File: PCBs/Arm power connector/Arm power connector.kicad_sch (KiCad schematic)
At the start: 11 parts, among them J1 Conn_01x08, J2 Conn_01x02

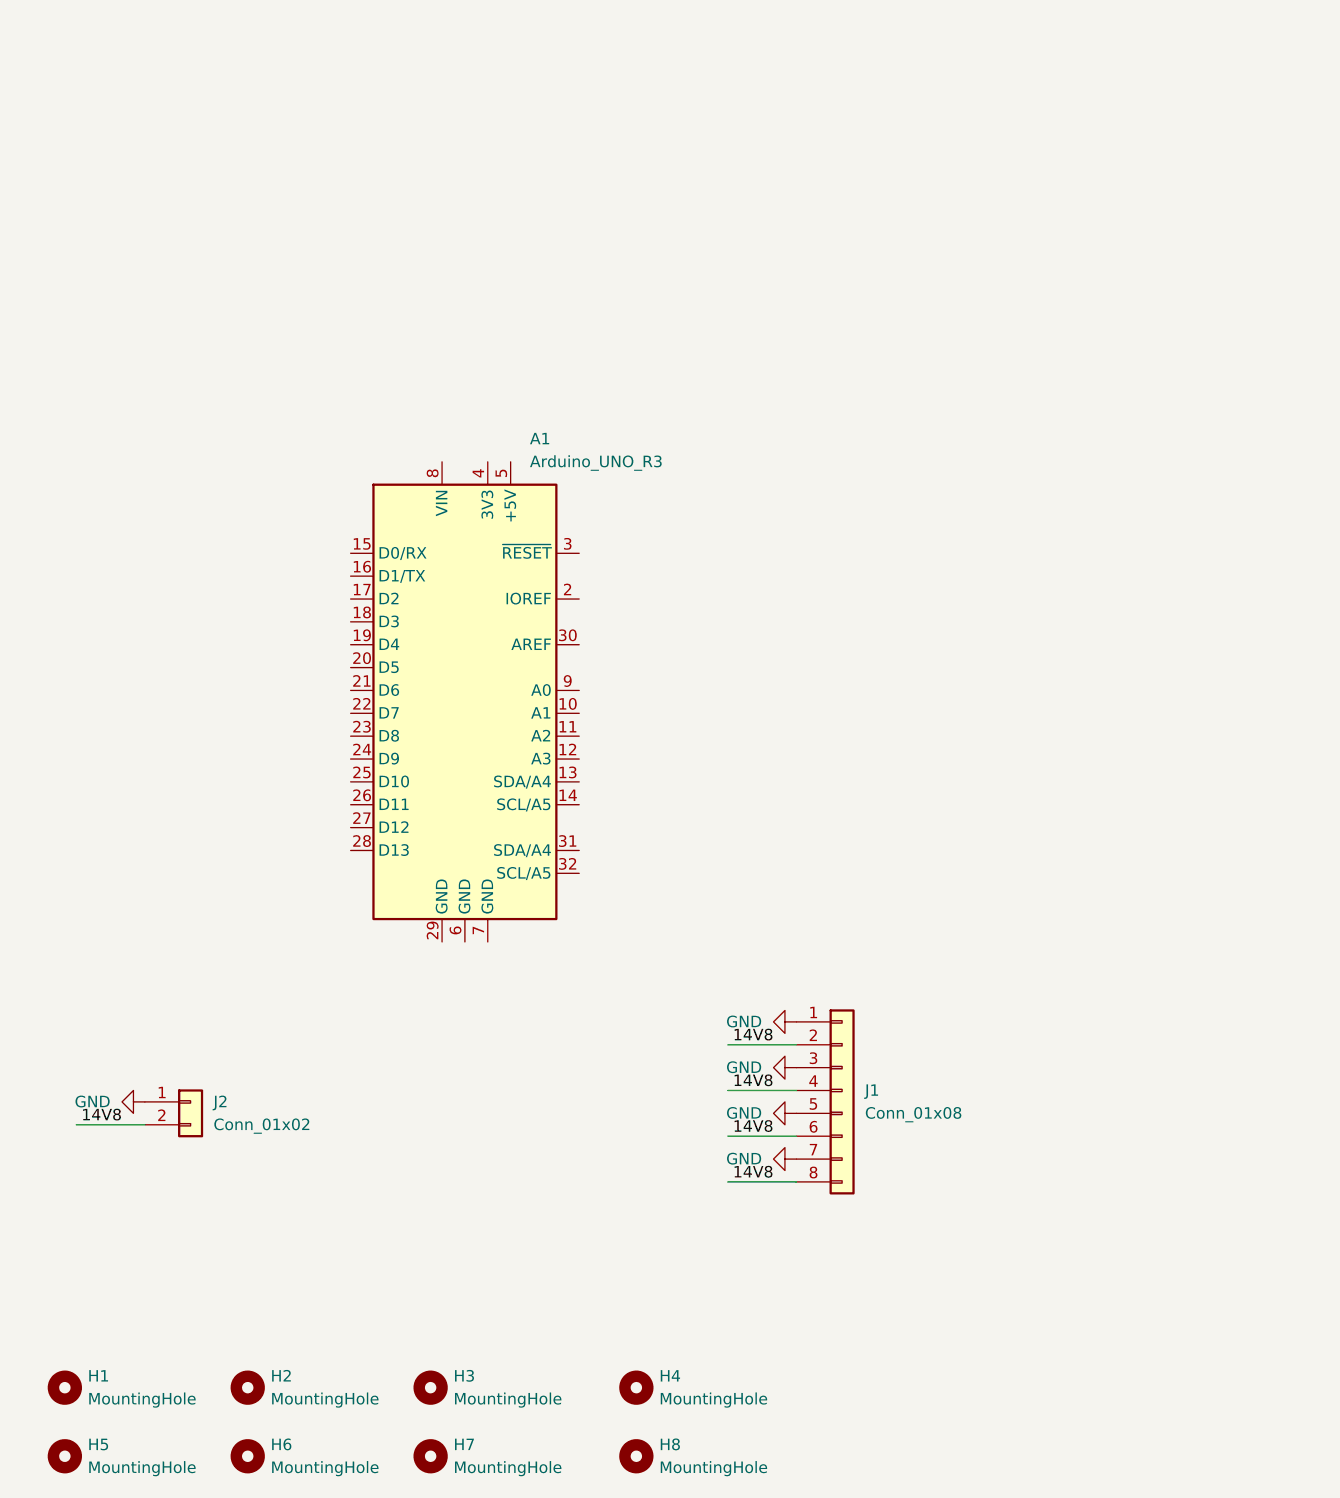
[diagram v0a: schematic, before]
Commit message: DRC clean arm connector layout
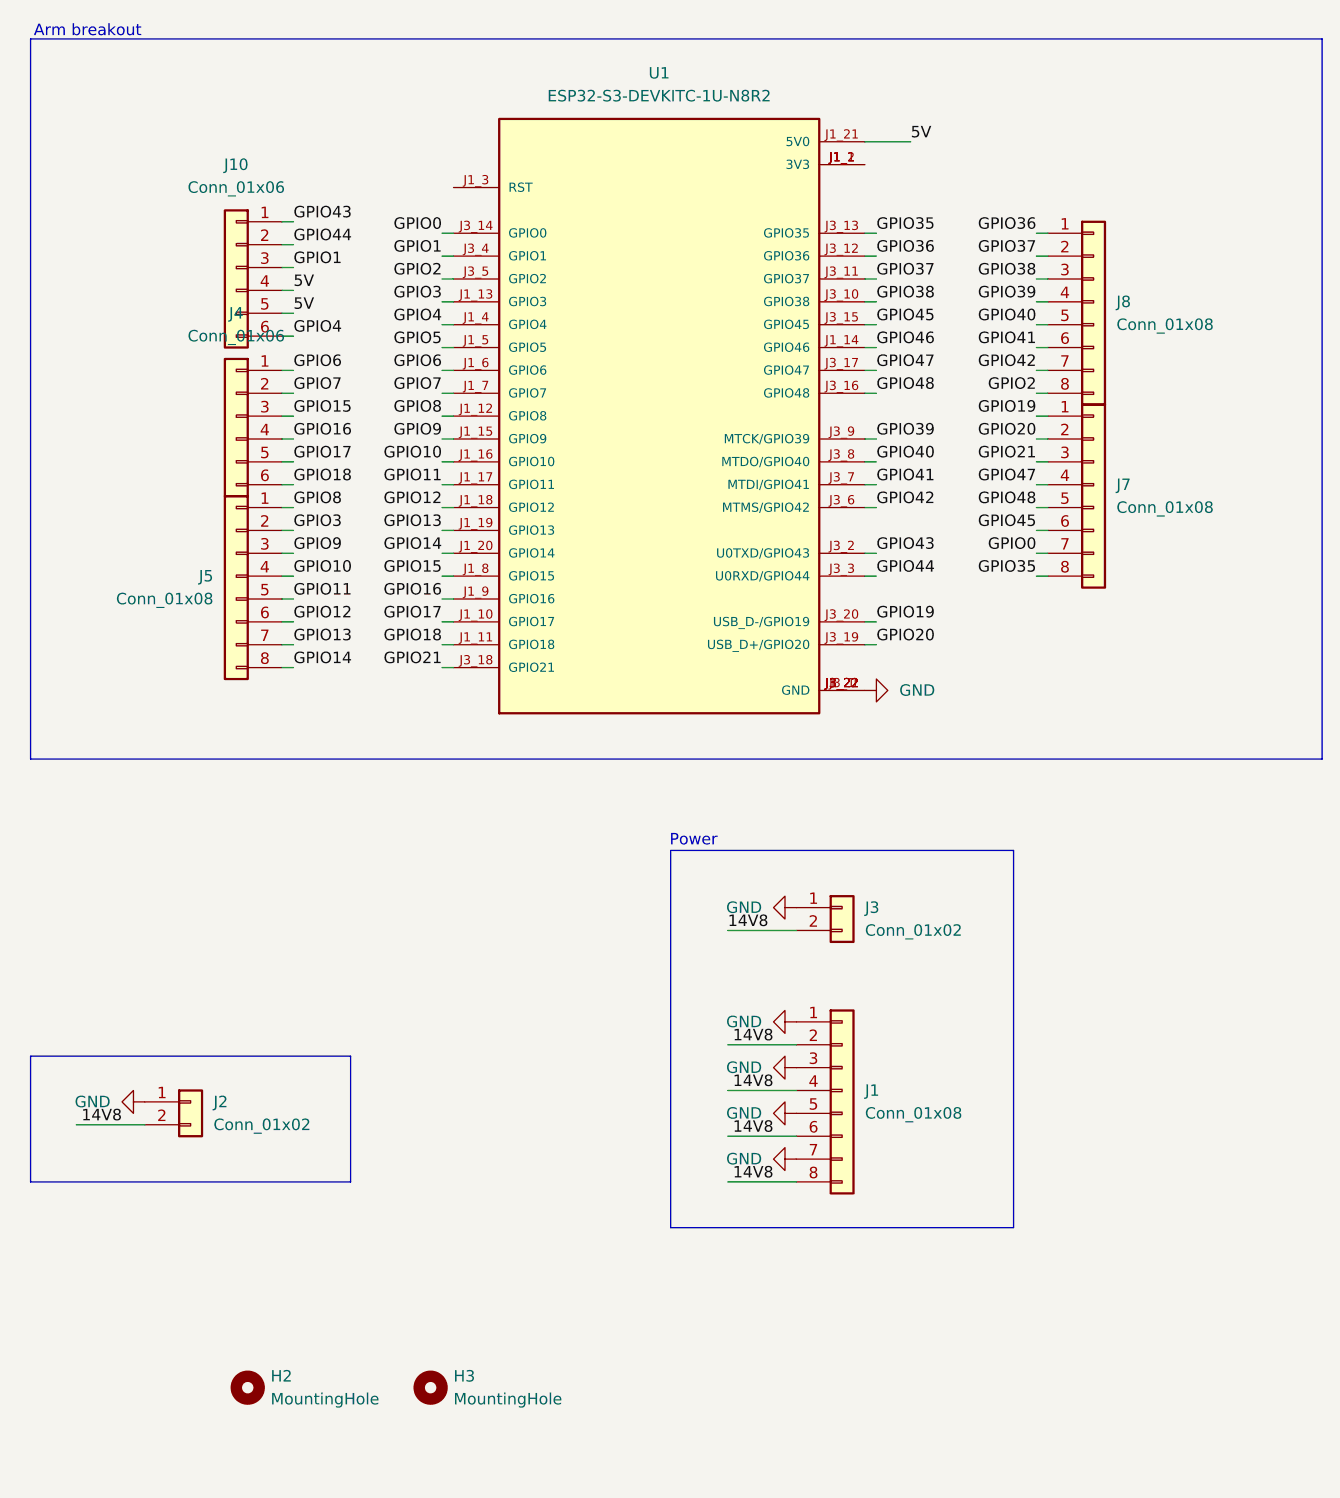
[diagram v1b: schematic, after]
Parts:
- removed A1: Arduino_UNO_R3, Module:Arduino_UNO_R3, symbol MCU_Module:Arduino_UNO_R3
- removed H1, H4, H5, H6, H7, H8: MountingHole, MountingHole:MountingHole_3.2mm_M3, symbol Mechanical:MountingHole
- added J10, J4: Conn_01x06, TerminalBlock:TerminalBlock_MaiXu_MX126-5.0-06P_1x06_P5.00mm, symbol Connector_Generic:Conn_01x06
- added J3: Conn_01x02, TerminalBlock:TerminalBlock_MaiXu_MX126-5.0-02P_1x02_P5.00mm, symbol Connector_Generic:Conn_01x02
- added J5, J7, J8: Conn_01x08, TerminalBlock:TerminalBlock_MaiXu_MX126-5.0-08P_1x08_P5.00mm, symbol Connector_Generic:Conn_01x08
- added U1: ESP32-S3-DEVKITC-1U-N8R2, IPRL_Footprints:XCVR_ESP32-S3-DEVKITC-1U-N8R2, symbol ESP32-S3-DEVKITC1:ESP32-S3-DEVKITC-1U-N8R2
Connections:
- net 14V8: now also J3.2 (Pin_2)
- net GND: now also J3.1 (Pin_1), U1.J1_22 (GND), U1.J3_1 (GND), U1.J3_21 (GND), U1.J3_22 (GND)
- new net: U1.J1_1 (3V3), U1.J1_2 (3V3)
- new net 5V: J10.4 (Pin_4), J10.5 (Pin_5), U1.J1_21 (5V0)
- new net GPIO0: J7.7 (Pin_7), U1.J3_14 (GPIO0)
- new net GPIO1: J10.3 (Pin_3), U1.J3_4 (GPIO1)
- new net GPIO10: J5.4 (Pin_4), U1.J1_16 (GPIO10)
- new net GPIO11: J5.5 (Pin_5), U1.J1_17 (GPIO11)
- new net GPIO12: J5.6 (Pin_6), U1.J1_18 (GPIO12)
- new net GPIO13: J5.7 (Pin_7), U1.J1_19 (GPIO13)
- new net GPIO14: J5.8 (Pin_8), U1.J1_20 (GPIO14)
- new net GPIO15: J4.3 (Pin_3), U1.J1_8 (GPIO15)
- new net GPIO16: J4.4 (Pin_4), U1.J1_9 (GPIO16)
- new net GPIO17: J4.5 (Pin_5), U1.J1_10 (GPIO17)
- new net GPIO18: J4.6 (Pin_6), U1.J1_11 (GPIO18)
- new net GPIO19: J7.1 (Pin_1), U1.J3_20 (USB_D-/GPIO19)
- new net GPIO2: J8.8 (Pin_8), U1.J3_5 (GPIO2)
- new net GPIO20: J7.2 (Pin_2), U1.J3_19 (USB_D+/GPIO20)
- new net GPIO21: J7.3 (Pin_3), U1.J3_18 (GPIO21)
- new net GPIO3: J5.2 (Pin_2), U1.J1_13 (GPIO3)
- new net GPIO35: J7.8 (Pin_8), U1.J3_13 (GPIO35)
- new net GPIO36: J8.1 (Pin_1), U1.J3_12 (GPIO36)
- new net GPIO37: J8.2 (Pin_2), U1.J3_11 (GPIO37)
- new net GPIO38: J8.3 (Pin_3), U1.J3_10 (GPIO38)
- new net GPIO39: J8.4 (Pin_4), U1.J3_9 (MTCK/GPIO39)
- new net GPIO4: J10.6 (Pin_6), U1.J1_4 (GPIO4)
- new net GPIO40: J8.5 (Pin_5), U1.J3_8 (MTDO/GPIO40)
- new net GPIO41: J8.6 (Pin_6), U1.J3_7 (MTDI/GPIO41)
- new net GPIO42: J8.7 (Pin_7), U1.J3_6 (MTMS/GPIO42)
- new net GPIO43: J10.1 (Pin_1), U1.J3_2 (U0TXD/GPIO43)
- new net GPIO44: J10.2 (Pin_2), U1.J3_3 (U0RXD/GPIO44)
- new net GPIO45: J7.6 (Pin_6), U1.J3_15 (GPIO45)
- new net GPIO46: U1.J1_14 (GPIO46)
- new net GPIO47: J7.4 (Pin_4), U1.J3_17 (GPIO47)
- new net GPIO48: J7.5 (Pin_5), U1.J3_16 (GPIO48)
- new net GPIO5: U1.J1_5 (GPIO5)
- new net GPIO6: J4.1 (Pin_1), U1.J1_6 (GPIO6)
- new net GPIO7: J4.2 (Pin_2), U1.J1_7 (GPIO7)
- new net GPIO8: J5.1 (Pin_1), U1.J1_12 (GPIO8)
- new net GPIO9: J5.3 (Pin_3), U1.J1_15 (GPIO9)
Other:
- note added: "Arm breakout"
- note added: "Power"
